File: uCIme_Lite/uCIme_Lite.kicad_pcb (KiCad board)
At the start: 4 copper layers, 65 x 56 mm, 71 parts, among them J1 POWER_MODES, J11 SERIAL_MODE, J12 SERIAL_VOLTAGE_SELECT, J2 JACK_POWER_IN, J3 USB_POWER_IN, J4 USB_PC, J6 5V_ENABLE, J7 SERIAL_AND_GPIO, J8 JACK_POWER_OUT, J9 USB_POWER_OUT, Q1 BSS138, Q2 BUK7M27-80EX, Q3 BUK7M27-80EX, Q4 BSS138, Q5 BSS138, Q6 BSS138, Q7 BSS138, Q8 BSS138, U1 LM74502, U2 LM74502, U3 AP2204K-ADJ, U4 AP2204K-ADJ, U5 FT230XS, U6 TXB0104D

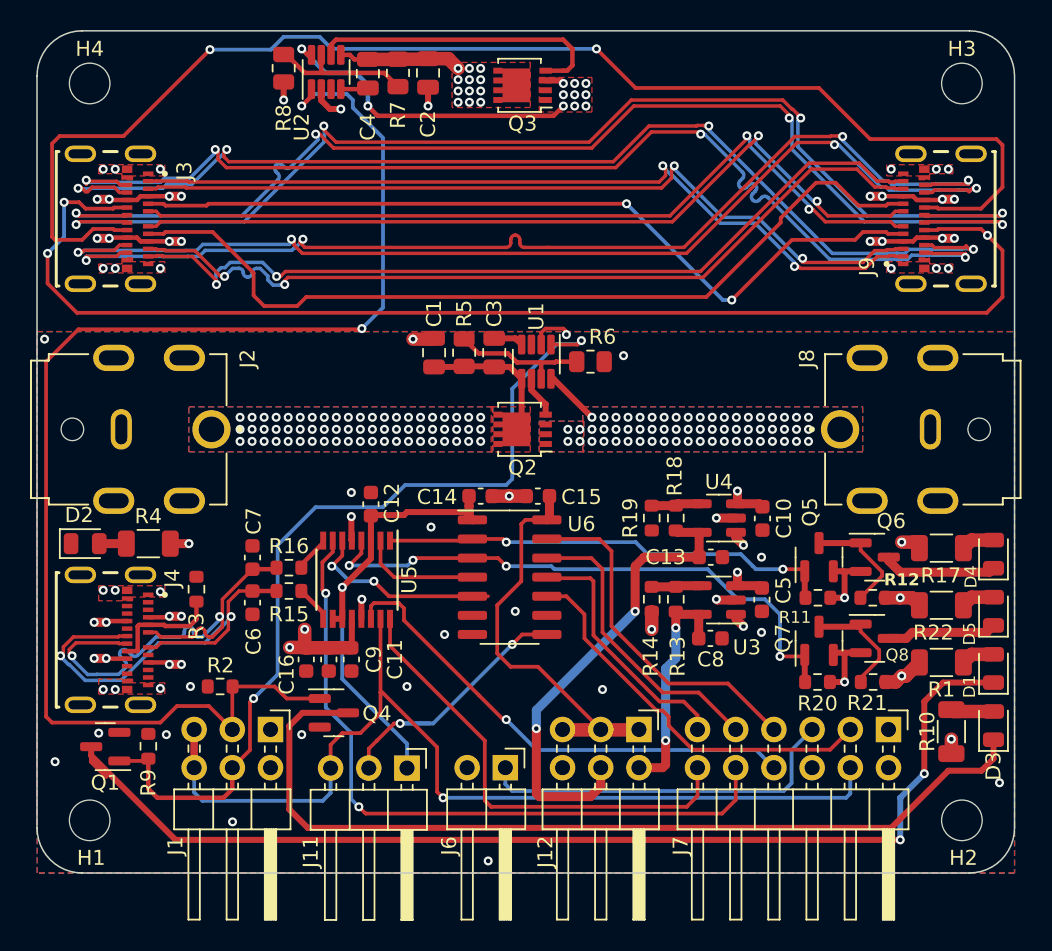
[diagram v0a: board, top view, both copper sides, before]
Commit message: lite: Fixed all PCB warnings.
Signed-off-by: Adrien Ricciardi <aricciardi@baylibre.com>
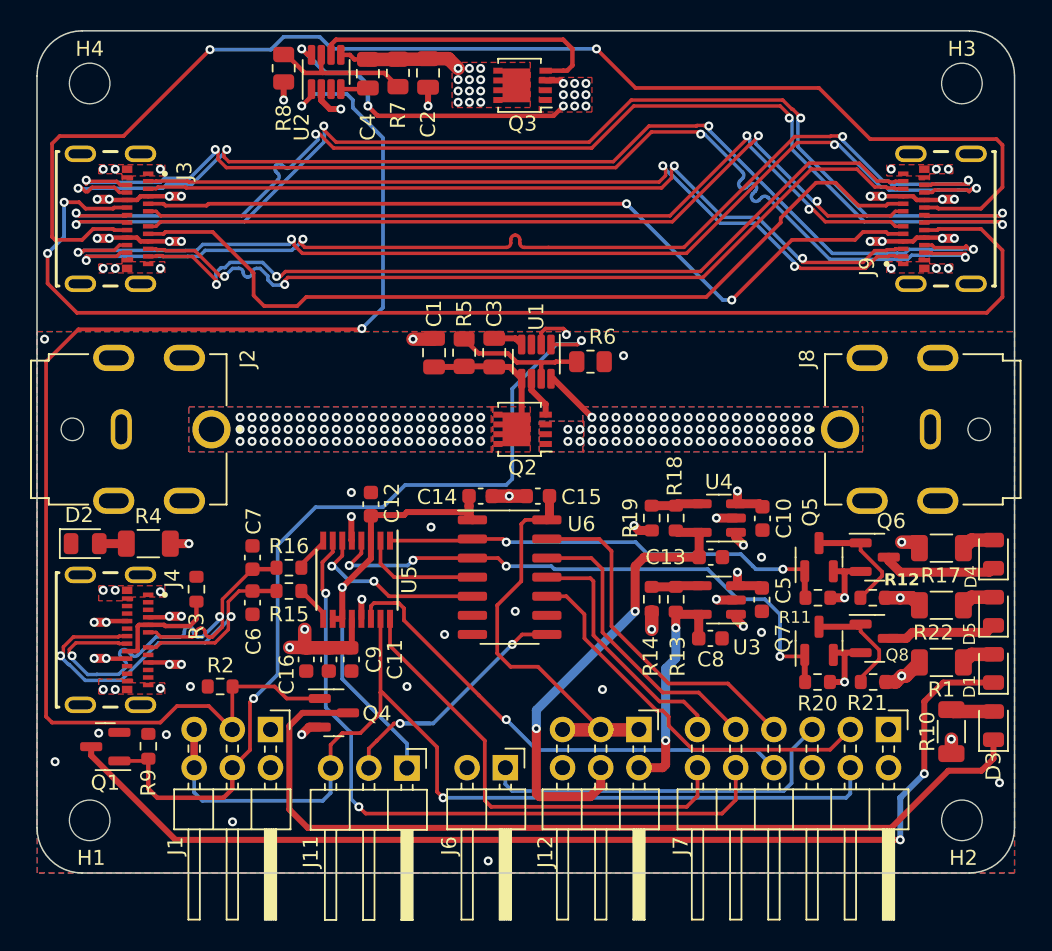
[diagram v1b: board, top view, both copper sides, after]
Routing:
- net GND: track 27.4 -> 30.1 mm, vias 49 -> 50
- net Net-(D1-K): track 74.1 -> 71.7 mm
- net Net-(U5-~{CTS}): track 13.2 -> 12.2 mm
- net /SBU2: vias 3 -> 2
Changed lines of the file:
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@@
   (segment (start 118.7 93.0375) (end 118.6 92.9375) (width 0.4) (layer "F.Cu") (net 2))
   (segment (start 86.5675 94.8325) (end 86.6 94.8) (width 0.4) (layer "F.Cu") (net 2))
+  (segment (start 105.025 90.225) (end 104.7 89.9) (width 0.6) (layer "F.Cu") (net 2))
   (segment (start 84.470038 62.2) (end 85.2 62.2) (width 0.4) (layer "F.Cu") (net 2))
   (segment (start 111.475 94.85) (end 110.225 94.85) (width 0.6) (layer "F.Cu") (net 2))
@@
   (segment (start 118.7 98.45) (end 118.6 98.35) (width 0.4) (layer "F.Cu") (net 2))
   (segment (start 110.225 94.85) (end 110.175 94.8) (width 0.6) (layer "F.Cu") (net 2))
+  (segment (start 83.1 103.3) (end 82.6 103.8) (width 0.6) (layer "F.Cu") (net 2))
   (segment (start 81.4 61.6) (end 81.4 60.4) (width 0.4) (layer "F.Cu") (net 2))
   (segment (start 98.525 77.075) (end 98.8 76.8) (width 0.25) (layer "F.Cu") (net 2))
   (segment (start 96.4 87.94) (end 95.275 87.94) (width 0.9) (layer "F.Cu") (net 2))
   (segment (start 85.9 90.8675) (end 85.9325 90.9) (width 0.4) (layer "F.Cu") (net 2))
+  (segment (start 83.8 103.3) (end 83.1 103.3) (width 0.6) (layer "F.Cu") (net 2))
   (segment (start 105.875 95.625) (end 105.875 96.8) (width 0.9) (layer "F.Cu") (net 2))
   (segment (start 100 76.8) (end 100.2 77) (width 0.25) (layer "F.Cu") (net 2))
+  (segment (start 118.7 94.7) (end 117.75 94.7) (width 0.6) (layer "F.Cu") (net 2))
   (segment (start 96.4 87.94) (end 97.525 87.94) (width 0.9) (layer "F.Cu") (net 2))
   (segment (start 118.1 98.35) (end 117.95 98.5) (width 0.4) (layer "F.Cu") (net 2))
@@
   (segment (start 98.525 77.8625) (end 98.525 77.075) (width 0.25) (layer "F.Cu") (net 2))
   (segment (start 91.35 77.5) (end 91.4 77.45) (width 0.9) (layer "F.Cu") (net 2))
-  (segment (start 118.7 94.7) (end 117.75 94.7) (width 0.4) (layer "F.Cu") (net 2))
   (segment (start 117.95 92.9375) (end 118.6 92.9375) (width 0.4) (layer "F.Cu") (net 2))
   (segment (start 91 62) (end 91 60.75) (width 0.4) (layer "F.Cu") (net 2))
@@
   (segment (start 90 77.5) (end 91.35 77.5) (width 0.9) (layer "F.Cu") (net 2))
   (segment (start 118.7 100.3) (end 117.725 100.3) (width 0.4) (layer "F.Cu") (net 2))
+  (segment (start 105.875 90.225) (end 105.025 90.225) (width 0.6) (layer "F.Cu") (net 2))
   (segment (start 118.6 98.35) (end 118.1 98.35) (width 0.4) (layer "F.Cu") (net 2))
   (via (at 118.7 100.3) (size 0.6) (drill 0.3) (layers "F.Cu" "B.Cu") (free) (net 2))
@@
   (via (at 129 107) (size 0.6) (drill 0.3) (layers "F.Cu" "B.Cu") (free) (net 2))
   (via (at 125.6 72.8) (size 0.6) (drill 0.3) (layers "F.Cu" "B.Cu") (free) (net 2))
+  (via (at 104.7 89.9) (size 0.6) (drill 0.3) (layers "F.Cu" "B.Cu") (free) (net 2))
   (via (at 100.2 77.2) (size 0.6) (drill 0.3) (layers "F.Cu" "B.Cu") (net 2))
   (via (at 92.1 97.14) (size 0.6) (drill 0.3) (layers "F.Cu" "B.Cu") (free) (net 2))
@@
   (segment (start 93.725 89.295) (end 93.95 89.52) (width 0.6) (layer "F.Cu") (net 9))
   (segment (start 93.725 87.94) (end 93.725 88.6) (width 0.6) (layer "F.Cu") (net 9))
-  (segment (start 87.2 89.25) (end 87.45 89) (width 0.4) (layer "F.Cu") (net 9))
   (segment (start 93.725 89) (end 93.725 89.295) (width 0.6) (layer "F.Cu") (net 9))
   (segment (start 89.4 89.2) (end 87.25 89.2) (width 0.4) (layer "F.Cu") (net 9))
@@
   (segment (start 128.6 100.3375) (end 125.2625 100.3375) (width 0.4) (layer "F.Cu") (net 12))
   (segment (start 125.2625 100.3375) (end 124 101.6) (width 0.4) (layer "F.Cu") (net 12))
-  (segment (start 68.6 105.6) (end 69.6 106.6) (width 0.3) (layer "F.Cu") (net 12))
   (segment (start 68.6 105.190317) (end 74.209683 110.8) (width 0.4) (layer "F.Cu") (net 12))
   (segment (start 68.6 104.6) (end 68.6 105.190317) (width 0.4) (layer "F.Cu") (net 12))
   (segment (start 124 101.6) (end 124 106.4) (width 0.4) (layer "F.Cu") (net 12))
   (segment (start 74.209683 110.8) (end 122.4 110.8) (width 0.4) (layer "F.Cu") (net 12))
-  (segment (start 68.6 104.6) (end 68.6 105.6) (width 0.3) (layer "F.Cu") (net 12))
   (via (at 124 106.4) (size 0.6) (drill 0.3) (layers "F.Cu" "B.Cu") (net 12))
   (via (at 122.4 110.8) (size 0.6) (drill 0.3) (layers "F.Cu" "B.Cu") (net 12))
@@
   (segment (start 67.8 68.4) (end 66.8 68.4) (width 0.25) (layer "F.Cu") (net 35))
   (segment (start 65.7 73.8) (end 65.7 71.8) (width 0.25) (layer "F.Cu") (net 35))
+  (segment (start 127.775 70.175) (end 129.2 71.6) (width 0.25) (layer "F.Cu") (net 35))
   (segment (start 68.225 68.825) (end 67.8 68.4) (width 0.25) (layer "F.Cu") (net 35))
   (segment (start 124 70.25) (end 124.866116 70.25) (width 0.25) (layer "F.Cu") (net 35))
@@
   (segment (start 129.2 74.7) (end 128.15 75.75) (width 0.25) (layer "F.Cu") (net 35))
   (segment (start 128.15 75.75) (end 67.65 75.75) (width 0.25) (layer "F.Cu") (net 35))
-  (segment (start 128.2 70.6) (end 129.2 71.6) (width 0.25) (layer "F.Cu") (net 35))
   (segment (start 124.866116 70.25) (end 124.941116 70.175) (width 0.25) (layer "F.Cu") (net 35))
   (segment (start 129.2 71.6) (end 129.2 74.7) (width 0.25) (layer "F.Cu") (net 35))
   (segment (start 70.99 68.75) (end 70.133884 68.75) (width 0.25) (layer "F.Cu") (net 35))
-  (segment (start 127.775 70.175) (end 128.2 70.6) (width 0.25) (layer "F.Cu") (net 35))
   (via (at 65.7 71.8) (size 0.6) (drill 0.3) (layers "F.Cu" "B.Cu") (net 35))
-  (via (at 128.2 70.6) (size 0.6) (drill 0.3) (layers "F.Cu" "B.Cu") (net 35))
   (via (at 66.8 68.4) (size 0.6) (drill 0.3) (layers "F.Cu" "B.Cu") (net 35))
   (segment (start 66.8 70.7) (end 66.8 68.4) (width 0.25) (layer "B.Cu") (net 35))
@@
   (segment (start 87.8375 92.424962) (end 87.8375 90.9) (width 0.25) (layer "F.Cu") (net 73))
   (segment (start 88.742538 93.33) (end 87.8375 92.424962) (width 0.25) (layer "F.Cu") (net 73))
-  (segment (start 93.95 94.6) (end 95 94.6) (width 0.23) (layer "F.Cu") (net 74))
   (segment (start 85.2975 90.9) (end 85.2975 91.9025) (width 0.25) (layer "F.Cu") (net 74))
   (segment (start 88.4 94.6) (end 87.4 93.6) (width 0.25) (layer "F.Cu") (net 74))
@@
     (connect_pads (clearance 0.5))
     (min_thickness 0.25) (filled_areas_thickness no)
-    (fill yes (thermal_gap 0.5) (thermal_bridge_width 0.5) (island_removal_mode 1) (island_area_min 10))
+    (fill yes (thermal_gap 0.5) (thermal_bridge_width 0.5))
     (polygon
       (pts
@@
     (connect_pads yes (clearance 0.5))
     (min_thickness 0.25) (filled_areas_thickness no)
-    (fill yes (thermal_gap 0.5) (thermal_bridge_width 0.5) (island_removal_mode 1) (island_area_min 10))
+    (fill yes (thermal_gap 0.5) (thermal_bridge_width 0.5))
     (polygon
       (pts
